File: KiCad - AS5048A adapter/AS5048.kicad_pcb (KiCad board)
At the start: 2 copper layers, 18.2 x 19.5 mm, 6 parts, among them J1 Conn_01x07_Socket

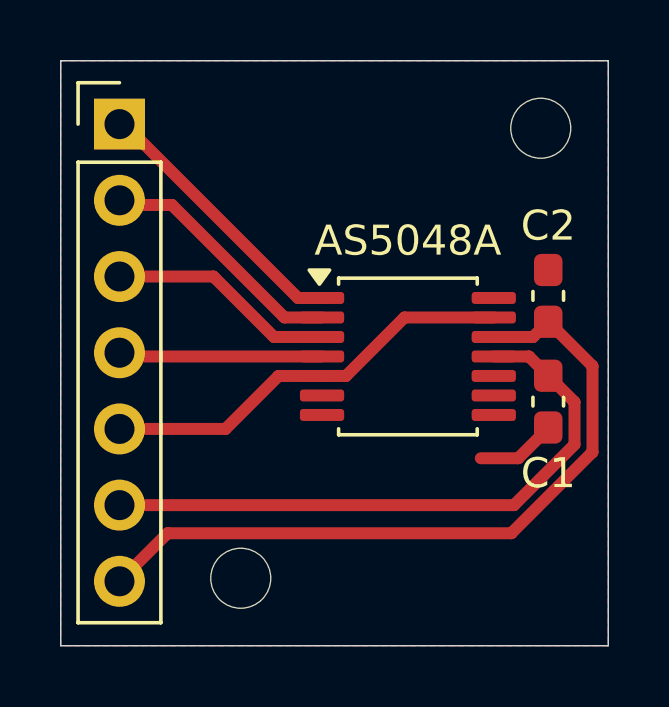
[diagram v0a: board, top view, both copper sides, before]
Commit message: BOM, pcbway stuff, and final check over
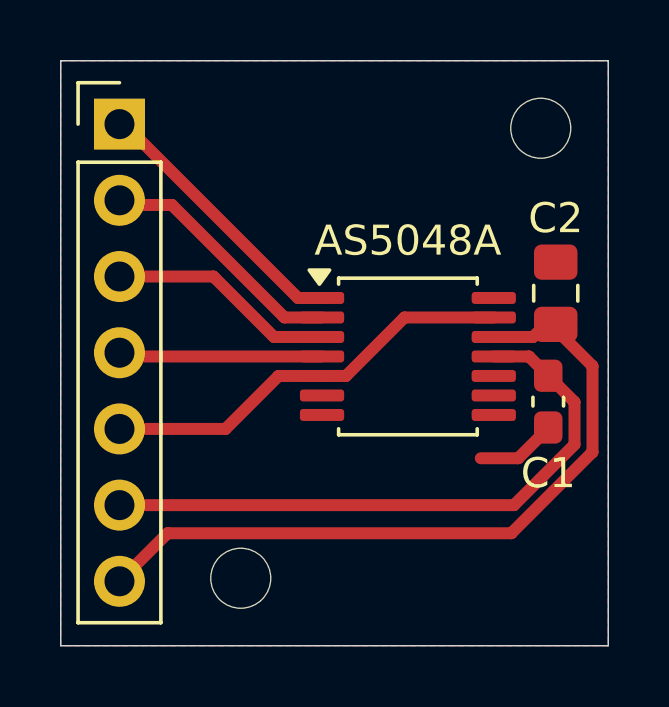
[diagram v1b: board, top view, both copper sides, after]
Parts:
- C2: footprint Capacitor_SMD:C_0603_1608Metric_Pad1.08x0.95mm_HandSolder -> Capacitor_SMD:C_0805_2012Metric_Pad1.18x1.45mm_HandSolder
- moved C2 0.26 mm to (76.5, 76.5)
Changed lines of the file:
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@@
 			(outputformat 1)
 			(mirror no)
-			(drillshape 1)
+			(drillshape 0)
 			(scaleselection 1)
 			(outputdirectory "")
@@
 			)
 		)
+		(property "Link" ""
+			(at 0 0 90)
+			(unlocked yes)
+			(layer "F.Fab")
+			(hide yes)
+			(effects
+				(font
+					(size 1 1)
+					(thickness 0.15)
+				)
+			)
+		)
+		(property "MANUFACTURER" "Murata Electronics"
+			(at 0 0 90)
+			(unlocked yes)
+			(layer "F.Fab")
+			(hide yes)
+			(effects
+				(font
+					(size 1 1)
+					(thickness 0.15)
+				)
+			)
+		)
+		(property "Manufacturer Part #" "GCM188L81H104KA57D"
+			(at 0 0 90)
+			(unlocked yes)
+			(layer "F.Fab")
+			(hide yes)
+			(effects
+				(font
+					(size 1 1)
+					(thickness 0.15)
+				)
+			)
+		)
+		(property "Price" ""
+			(at 0 0 90)
+			(unlocked yes)
+			(layer "F.Fab")
+			(hide yes)
+			(effects
+				(font
+					(size 1 1)
+					(thickness 0.15)
+				)
+			)
+		)
 		(property ki_fp_filters "C_*")
 		(sheetname "/")
 		(sheetfile "AS5048.kicad_sch")
+		(units
+			(unit
+				(name "A")
+				(pins "1" "2")
+			)
+		)
 		(attr smd)
 		(duplicate_pad_numbers_are_jumpers no)
@@
 		)
 	)
-	(footprint "Capacitor_SMD:C_0603_1608Metric_Pad1.08x0.95mm_HandSolder"
+	(footprint "Capacitor_SMD:C_0805_2012Metric_Pad1.18x1.45mm_HandSolder"
 		(layer "F.Cu")
-		(at 76.25 76.5875 90)
-		(descr "Capacitor SMD 0603 (1608 Metric), square (rectangular) end terminal, IPC-7351 nominal with elongated pad for handsoldering. (Body size source: IPC-SM-782 page 76, https://www.pcb-3d.com/wordpress/wp-content/uploads/ipc-sm-782a_amendment_1_and_2.pdf)")
+		(at 76.5 76.5 90)
+		(descr "Capacitor SMD 0805 (2012 Metric), square (rectangular) end terminal, IPC-7351 nominal with elongated pad for handsoldering. (Body size source: IPC-SM-782 page 76, https://www.pcb-3d.com/wordpress/wp-content/uploads/ipc-sm-782a_amendment_1_and_2.pdf, https://docs.google.com/spreadsheets/d/1BsfQQcO9C6DZCsRaXUlFlo91Tg2WpOkGARC1WS5S8t0/edit?usp=sharing)")
 		(tags "capacitor handsolder")
 		(property "Reference" "C2"
-			(at 2.3375 0 180)
+			(at 2.5 0 180)
 			(layer "F.SilkS")
 			(effects
@@
 		)
 		(property "Value" "10uF"
-			(at 0 1.43 90)
+			(at 0 1.68 90)
 			(layer "F.Fab")
 			(hide yes)
@@
 			(at 0 0 90)
 			(layer "F.SilkS")
+			(hide yes)
+			(effects
+				(font
+					(size 1 1)
+					(thickness 0.15)
+				)
+			)
+		)
+		(property "Link" ""
+			(at 0 0 90)
+			(unlocked yes)
+			(layer "F.Fab")
+			(hide yes)
+			(effects
+				(font
+					(size 1 1)
+					(thickness 0.15)
+				)
+			)
+		)
+		(property "MANUFACTURER" "Murata Electronics"
+			(at 0 0 90)
+			(unlocked yes)
+			(layer "F.Fab")
+			(hide yes)
+			(effects
+				(font
+					(size 1 1)
+					(thickness 0.15)
+				)
+			)
+		)
+		(property "Manufacturer Part #" "GCJ21BR71A106KE01L"
+			(at 0 0 90)
+			(unlocked yes)
+			(layer "F.Fab")
+			(hide yes)
+			(effects
+				(font
+					(size 1 1)
+					(thickness 0.15)
+				)
+			)
+		)
+		(property "Price" ""
+			(at 0 0 90)
+			(unlocked yes)
+			(layer "F.Fab")
 			(hide yes)
 			(effects
@@
 		(sheetname "/")
 		(sheetfile "AS5048.kicad_sch")
+		(units
+			(unit
+				(name "A")
+				(pins "1" "2")
+			)
+		)
 		(attr smd)
 		(duplicate_pad_numbers_are_jumpers no)
 		(fp_line
-			(start -0.146267 -0.51)
-			(end 0.146267 -0.51)
+			(start -0.261252 -0.735)
+			(end 0.261252 -0.735)
 			(stroke
 				(width 0.12)
@@
 		)
 		(fp_line
-			(start -0.146267 0.51)
-			(end 0.146267 0.51)
+			(start -0.261252 0.735)
+			(end 0.261252 0.735)
 			(stroke
 				(width 0.12)
@@
 		)
 		(fp_rect
-			(start -1.65 -0.73)
-			(end 1.65 0.73)
+			(start -1.88 -0.98)
+			(end 1.88 0.98)
 			(stroke
 				(width 0.05)
@@
 		)
 		(fp_rect
-			(start -0.8 -0.4)
-			(end 0.8 0.4)
+			(start -1 -0.625)
+			(end 1 0.625)
 			(stroke
 				(width 0.1)
@@
 			(effects
 				(font
-					(size 0.4 0.4)
-					(thickness 0.06)
+					(size 0.5 0.5)
+					(thickness 0.08)
 				)
 			)
 		)
 		(pad "1" smd roundrect
-			(at -0.8625 0 90)
-			(size 1.075 0.95)
-			(layers "F.Cu" "F.Mask" "F.Paste")
-			(roundrect_rratio 0.25)
+			(at -1.0375 0 90)
+			(size 1.175 1.45)
+			(layers "F.Cu" "F.Mask" "F.Paste")
+			(roundrect_rratio 0.212766)
 			(net "+3V3")
 			(pintype "passive")
 		)
 		(pad "2" smd roundrect
-			(at 0.8625 0 90)
-			(size 1.075 0.95)
-			(layers "F.Cu" "F.Mask" "F.Paste")
-			(roundrect_rratio 0.25)
+			(at 1.0375 0 90)
+			(size 1.175 1.45)
+			(layers "F.Cu" "F.Mask" "F.Paste")
+			(roundrect_rratio 0.212766)
 			(net "GND")
 			(pintype "passive")
 		)
 		(embedded_fonts no)
-		(model "${KICAD10_3DMODEL_DIR}/Capacitor_SMD.3dshapes/C_0603_1608Metric.step"
+		(model "${KICAD10_3DMODEL_DIR}/Capacitor_SMD.3dshapes/C_0805_2012Metric.step"
 			(offset
 				(xyz 0 0 0)
@@
 			(hide yes)
 			(effects
+				(font
+					(size 1 1)
+					(thickness 0.15)
+				)
+			)
+		)
+		(property "Link" ""
+			(at 0 0 0)
+			(unlocked yes)
+			(layer "F.Fab")
+			(hide yes)
+			(effects
+				(font
+					(size 1 1)
+					(thickness 0.15)
+				)
+			)
+		)
+		(property "MANUFACTURER" ""
+			(at 0 0 0)
+			(unlocked yes)
+			(layer "F.Fab")
+			(hide yes)
+			(effects
+				(font
+					(size 1 1)
+					(thickness 0.15)
+				)
+			)
+		)
+		(property "Manufacturer Part #" ""
+			(at 0 0 0)
+			(unlocked yes)
+			(layer "F.Fab")
+			(hide yes)
+			(effects
+				(font
+					(size 1 1)
+					(thickness 0.15)
+				)
+			)
+		)
+		(property "Price" ""
+			(at 0 0 0)
+			(unlocked yes)
+			(layer "F.Fab")
+			(hide yes)
+			(effects
